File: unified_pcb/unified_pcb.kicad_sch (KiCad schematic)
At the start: 102 parts, among them J1 Conn_01x02_Socket, J2 USB_C_Receptacle, J3 Conn_01x02_Socket, J4 Conn_01x03_Pin, Q1 Q_Photo_NPN, Q2 Q_Photo_NPN, Q3 Q_Photo_NPN, SW1 SW_Push, SW2 SW_Push, U1 BQ27427YZFR, U10 3.3V LDO, U11 LMD4030T261-OA1, U12 LY4176D, U2 USBLC6-2P6, U3 RS0302, U4 RP2350_60QFN, U5 TLV7113318DDSER, U7 QSPI Flash, U8 TPGLF72101CSP4, U9 ICM-20948, Y1 12MHz

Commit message: wow ICM_20948 is moving out of production and is expensive - move to BMI270+MMC5603NJ, no need anymore for 1.8V net at all, possibly drop the second ldo entirely for mosfets vs just use a second RT9078 but my haiku is threatened and feeling confused attachment because of this
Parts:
- removed C57: snub, Capacitor_SMD:C_0402_1005Metric, symbol Device:C_Small
- removed R26, R27, R34: 4.7k, Resistor_SMD:R_0402_1005Metric, symbol Device:R_Small
- removed U3: RS0302, Package_SON:X2SON-8_1.4x1mm_P0.35mm, symbol motionhexa:RS0302
- added C48: 1uF, Capacitor_SMD:C_0402_1005Metric, symbol Device:C_Small
- added C63: 2.2uF, Capacitor_SMD:C_0402_1005Metric, symbol Device:C_Small
- added C64, C65: 100nF, Capacitor_SMD:C_0402_1005Metric, symbol Device:C_Small
- added Q4: AO3401A, Package_TO_SOT_SMD:SOT-23, symbol Transistor_FET:AO3401A
- added Q5: 2N7002, Package_TO_SOT_SMD:SOT-23, symbol Transistor_FET:2N7002
- added U13: MMC5603NJ, motionhexa:MMC5603NJ_WLP-4_0.8x0.8mm_P0.4mm, symbol motionhexa:MMC5603NJ
- added U14: BMI270, Package_LGA:Bosch_LGA-14_3x2.5mm_P0.5mm, symbol motionhexa:BMI270
- added U3: 3.3V LDO, Package_DFN_QFN:OnSemi_XDFN4-1EP_1.0x1.0mm_EP0.52x0.52mm, symbol penta:RT9078-33GQZ
- C38: value 100nF -> 1uF; Designation CC0402KRX7R7BB104 -> CL05A105KP5NNNC; LCSC C60474 -> C14445
- C42, C43, C44, C54, C55, C56, U5, U9: now not fitted; now left out of the parts list
- R25: value 200k -> 33k; Designation (none) -> 0402WGF3302TCE; LCSC (none) -> C25779
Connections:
- net +3V3: now also C48.1, C63.1, C64.1, C65.1, U13.B1 (VDD), U14.5 (VDDIO), U14.8 (VDD), U3.1 (VOUT); no longer R25.2
- net -BATT: now also C38.2, R25.2, C48.2, C63.2, C64.2, C65.2, U13.A1 (VSA), U14.6 (GNDIO), U14.7 (GND), U3.2 (GND), U3.5 (SGND); no longer C38.1
- net EN_CHARGE: now also U4.7 (GPIO4); no longer U4.4 (GPIO2)
- net EN_LDO: now also R25.1, U3.3 (EN)
- net MOTION_INT: now also U4.8 (GPIO5), U14.4 (INT1); no longer U4.2 (GPIO0)
- net SCL_3V3: now also U13.A2 (SCL)
- net SDA_3V3: now also U13.B2 (SDA)
- net VDD: now also C38.1, U3.4 (VIN)
- net IMU_CS: now reaches U4.3 (GPIO1)
- net IMU_CS: now also U14.12 (CSB)
- net IMU_MOSI: now reaches U4.5 (GPIO3)
- net IMU_MOSI: now also U14.14 (SDx)
- new net IMU_MISO: U14.1 (SDO), U4.2 (GPIO0)
- new net IMU_SCK: U14.13 (SCx), U4.4 (GPIO2)
- no-connect marks 24 -> 25
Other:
- note added: "3.3V regulator"
- note added: "autobrightness plz work"
- note added: "lipo charger"
- note added: "magnetic sensor"
- note removed: "3.3V and 1.8V regulator"
- note removed: "Battery Sense divider: 4.2V => 2.62V read 3.7V => 2.30V read 3.2V => 1.99V read"
- note removed: "CHECK TAPE ORIENTATION"
- note removed: "SDA/SCL swapped for U3 layout"
- note removed: "jumper bridged: button-mode"
- note removed: "optional in case panel power voltage drop impacts LDO"
- moved on the sheet: C58, C59, C60, C61, C62, DD10, DD6, DD7, DD8, DD9, R14, R15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

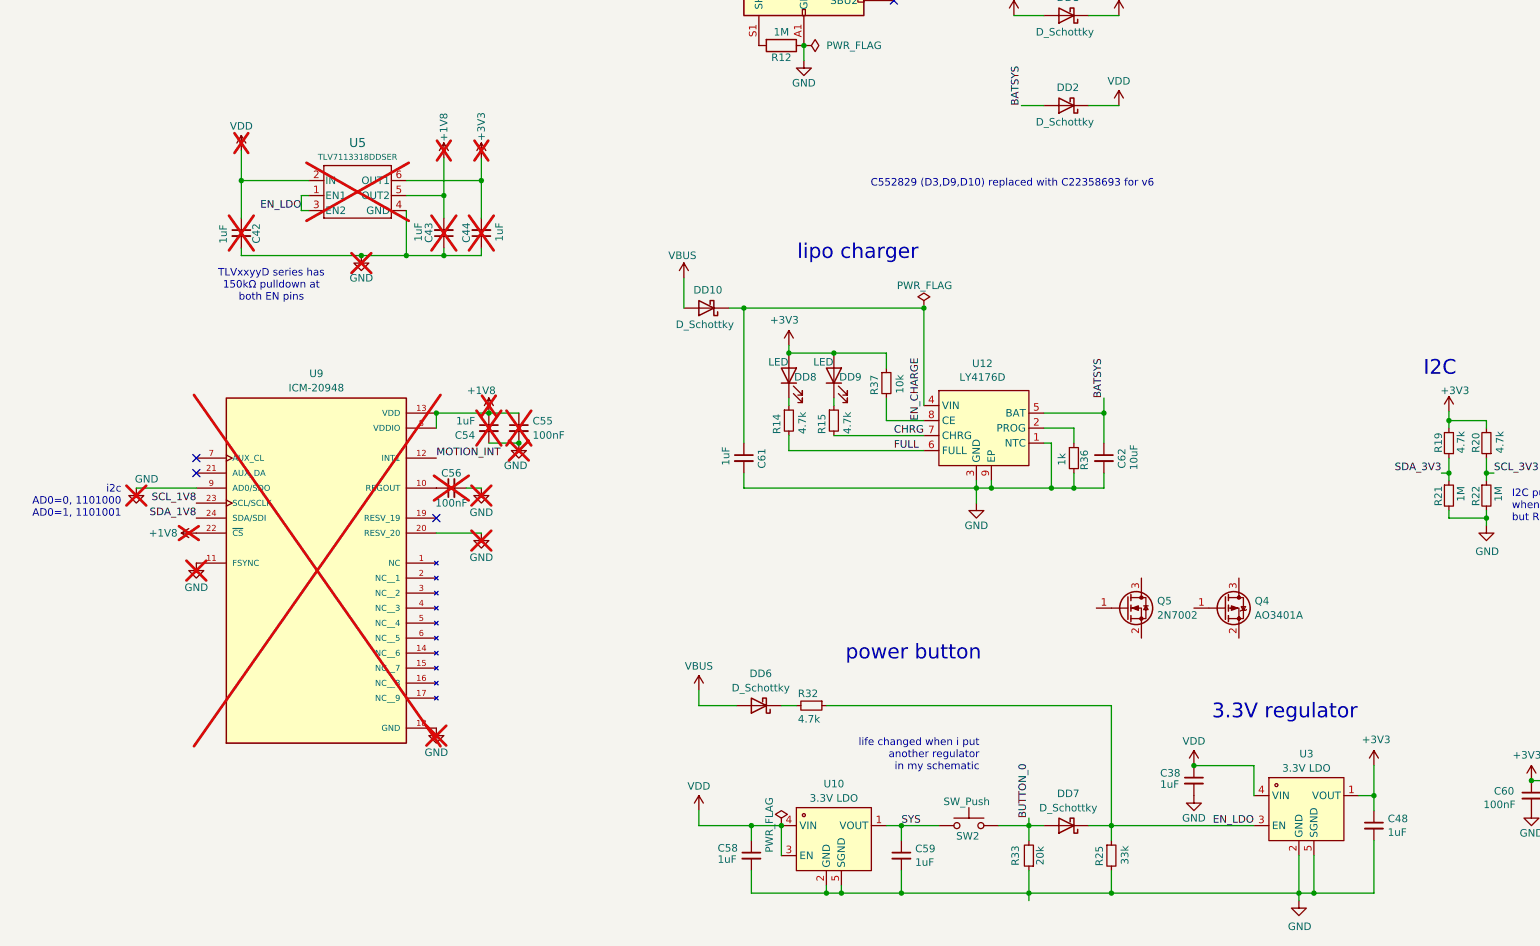
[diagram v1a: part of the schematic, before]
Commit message: remove old schematic pieces, update schematic format?
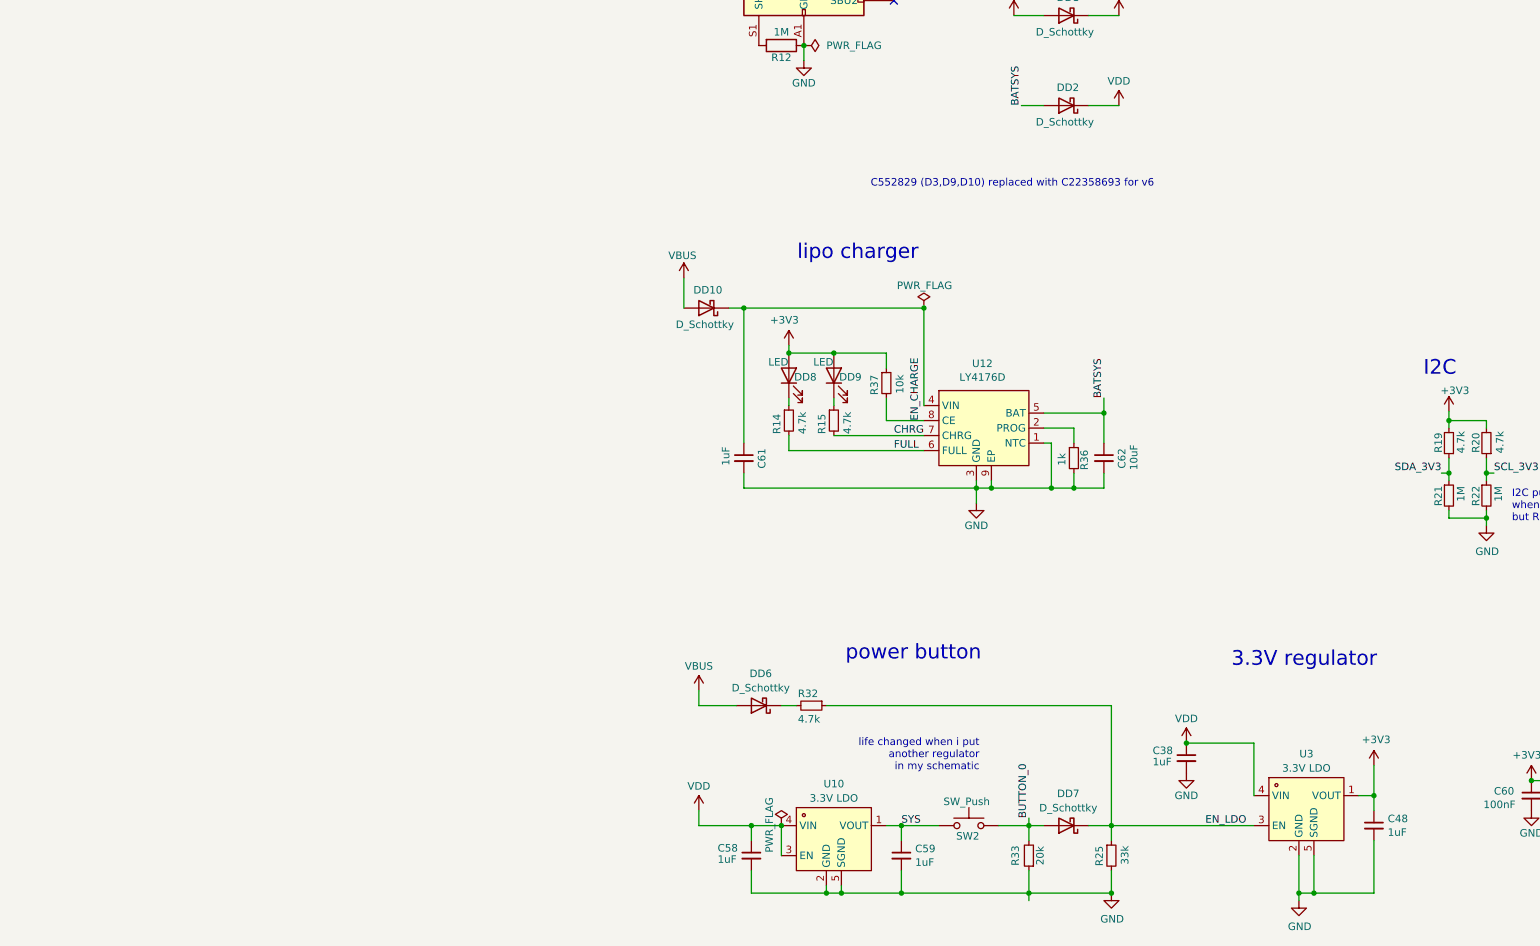
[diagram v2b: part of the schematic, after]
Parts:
- removed C42, C43, C44, C54: 1uF, Capacitor_SMD:C_0402_1005Metric, symbol Device:C_Small
- removed C55, C56: 100nF, Capacitor_SMD:C_0402_1005Metric, symbol Device:C_Small
- removed Q4: AO3401A, Package_TO_SOT_SMD:SOT-23, symbol Transistor_FET:AO3401A
- removed Q5: 2N7002, Package_TO_SOT_SMD:SOT-23, symbol Transistor_FET:2N7002
- removed U5: TLV7113318DDSER, Package_SON:WSON-6_1.5x1.5mm_P0.5mm, symbol motionhexa:TLV7111833DDSER
- removed U9: ICM-20948, motionhexa:QFN40P300X300X105-24N, symbol motionhexa:ICM-20948
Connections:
- no-connect marks 25 -> 22
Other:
- note removed: "TLVxxyyD series has 150kΩ pulldown at both EN pins"
- note removed: "i2c AD0=0, 1101000 AD0=1, 1101001"
- moved on the sheet: C38
